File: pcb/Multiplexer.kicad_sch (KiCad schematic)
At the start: 1 part, among them U2 TMUX1308

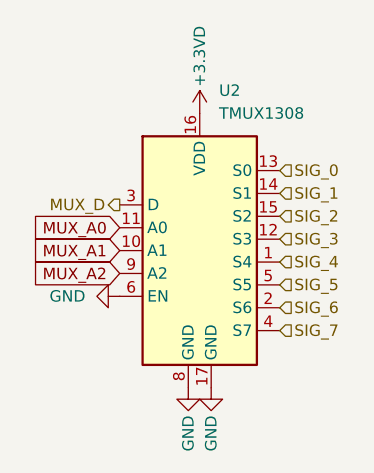
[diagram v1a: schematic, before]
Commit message: feat: assigned footprints for each symbol and switch
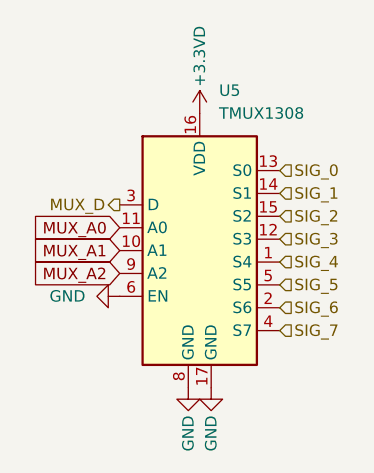
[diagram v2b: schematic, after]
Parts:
- renumbered U2 to U5
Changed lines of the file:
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@@
 		(on_board yes)
 		(dnp no)
-		(property "Reference" "#PWR05"
+		(property "Reference" "#PWR054"
 			(at 78.74 66.04 0)
 			(effects
@@
 			(project "prometheus-65"
 				(path "/7080535f-072d-4fc6-b033-a9cfe8594544/0adfa91a-0784-424f-9949-4c22152ab92f"
-					(reference "#PWR0513")
+					(reference "#PWR0448")
 					(unit 1)
 				)
 				(path "/7080535f-072d-4fc6-b033-a9cfe8594544/4aa91533-6d19-4b18-bd97-843bbf9a2ebd"
-					(reference "#PWR0517")
+					(reference "#PWR0452")
 					(unit 1)
 				)
 				(path "/7080535f-072d-4fc6-b033-a9cfe8594544/57499abe-bae0-4aba-b387-192b72537f00"
-					(reference "#PWR0285")
+					(reference "#PWR0252")
 					(unit 1)
 				)
 				(path "/7080535f-072d-4fc6-b033-a9cfe8594544/5fb3d5f1-a778-4ba7-9988-406cde0bb447"
-					(reference "#PWR0225")
+					(reference "#PWR0200")
 					(unit 1)
 				)
 				(path "/7080535f-072d-4fc6-b033-a9cfe8594544/8fd9d515-2105-4930-9563-b36413125d29"
-					(reference "#PWR0165")
+					(reference "#PWR0148")
 					(unit 1)
 				)
 				(path "/7080535f-072d-4fc6-b033-a9cfe8594544/a9c42e61-5ec1-4fa9-ae2f-cdc1de1fa9fe"
-					(reference "#PWR05")
+					(reference "#PWR054")
 					(unit 1)
 				)
 				(path "/7080535f-072d-4fc6-b033-a9cfe8594544/ea62a3f7-6568-4743-86d5-db015650f22d"
-					(reference "#PWR0521")
+					(reference "#PWR0456")
 					(unit 1)
 				)
 				(path "/7080535f-072d-4fc6-b033-a9cfe8594544/f2e1a5a1-adb9-4d0f-84af-2191946e6f18"
-					(reference "#PWR0525")
+					(reference "#PWR0460")
 					(unit 1)
 				)
@@
 		(dnp no)
 		(fields_autoplaced yes)
-		(property "Reference" "#PWR06"
+		(property "Reference" "#PWR055"
 			(at 63.5 82.55 0)
 			(effects
@@
 			(project "prometheus-65"
 				(path "/7080535f-072d-4fc6-b033-a9cfe8594544/0adfa91a-0784-424f-9949-4c22152ab92f"
-					(reference "#PWR0511")
+					(reference "#PWR0449")
 					(unit 1)
 				)
 				(path "/7080535f-072d-4fc6-b033-a9cfe8594544/4aa91533-6d19-4b18-bd97-843bbf9a2ebd"
-					(reference "#PWR0515")
+					(reference "#PWR0453")
 					(unit 1)
 				)
 				(path "/7080535f-072d-4fc6-b033-a9cfe8594544/57499abe-bae0-4aba-b387-192b72537f00"
-					(reference "#PWR0283")
+					(reference "#PWR0253")
 					(unit 1)
 				)
 				(path "/7080535f-072d-4fc6-b033-a9cfe8594544/5fb3d5f1-a778-4ba7-9988-406cde0bb447"
-					(reference "#PWR0223")
+					(reference "#PWR0201")
 					(unit 1)
 				)
 				(path "/7080535f-072d-4fc6-b033-a9cfe8594544/8fd9d515-2105-4930-9563-b36413125d29"
-					(reference "#PWR0163")
+					(reference "#PWR0149")
 					(unit 1)
 				)
 				(path "/7080535f-072d-4fc6-b033-a9cfe8594544/a9c42e61-5ec1-4fa9-ae2f-cdc1de1fa9fe"
-					(reference "#PWR06")
+					(reference "#PWR055")
 					(unit 1)
 				)
 				(path "/7080535f-072d-4fc6-b033-a9cfe8594544/ea62a3f7-6568-4743-86d5-db015650f22d"
-					(reference "#PWR0519")
+					(reference "#PWR0457")
 					(unit 1)
 				)
 				(path "/7080535f-072d-4fc6-b033-a9cfe8594544/f2e1a5a1-adb9-4d0f-84af-2191946e6f18"
-					(reference "#PWR0523")
+					(reference "#PWR0461")
 					(unit 1)
 				)
@@
 		(on_board yes)
 		(dnp no)
-		(property "Reference" "#PWR03"
+		(property "Reference" "#PWR056"
 			(at 77.47 99.06 0)
 			(effects
@@
 			(project "prometheus-65"
 				(path "/7080535f-072d-4fc6-b033-a9cfe8594544/0adfa91a-0784-424f-9949-4c22152ab92f"
-					(reference "#PWR0512")
+					(reference "#PWR0450")
 					(unit 1)
 				)
 				(path "/7080535f-072d-4fc6-b033-a9cfe8594544/4aa91533-6d19-4b18-bd97-843bbf9a2ebd"
-					(reference "#PWR0516")
+					(reference "#PWR0454")
 					(unit 1)
 				)
 				(path "/7080535f-072d-4fc6-b033-a9cfe8594544/57499abe-bae0-4aba-b387-192b72537f00"
-					(reference "#PWR0284")
+					(reference "#PWR0254")
 					(unit 1)
 				)
 				(path "/7080535f-072d-4fc6-b033-a9cfe8594544/5fb3d5f1-a778-4ba7-9988-406cde0bb447"
-					(reference "#PWR0224")
+					(reference "#PWR0202")
 					(unit 1)
 				)
 				(path "/7080535f-072d-4fc6-b033-a9cfe8594544/8fd9d515-2105-4930-9563-b36413125d29"
-					(reference "#PWR0164")
+					(reference "#PWR0150")
 					(unit 1)
 				)
 				(path "/7080535f-072d-4fc6-b033-a9cfe8594544/a9c42e61-5ec1-4fa9-ae2f-cdc1de1fa9fe"
-					(reference "#PWR03")
+					(reference "#PWR056")
 					(unit 1)
 				)
 				(path "/7080535f-072d-4fc6-b033-a9cfe8594544/ea62a3f7-6568-4743-86d5-db015650f22d"
-					(reference "#PWR0520")
+					(reference "#PWR0458")
 					(unit 1)
 				)
 				(path "/7080535f-072d-4fc6-b033-a9cfe8594544/f2e1a5a1-adb9-4d0f-84af-2191946e6f18"
-					(reference "#PWR0524")
+					(reference "#PWR0462")
 					(unit 1)
 				)
@@
 		(dnp no)
 		(fields_autoplaced yes)
-		(property "Reference" "U2"
+		(property "Reference" "U5"
 			(at 80.8833 59.69 0)
 			(effects
@@
 				)
 				(path "/7080535f-072d-4fc6-b033-a9cfe8594544/a9c42e61-5ec1-4fa9-ae2f-cdc1de1fa9fe"
-					(reference "U2")
+					(reference "U5")
 					(unit 1)
 				)
@@
 		(on_board yes)
 		(dnp no)
-		(property "Reference" "#PWR04"
+		(property "Reference" "#PWR057"
 			(at 80.01 99.06 0)
 			(effects
@@
 			(project "prometheus-65"
 				(path "/7080535f-072d-4fc6-b033-a9cfe8594544/0adfa91a-0784-424f-9949-4c22152ab92f"
-					(reference "#PWR0514")
+					(reference "#PWR0451")
 					(unit 1)
 				)
 				(path "/7080535f-072d-4fc6-b033-a9cfe8594544/4aa91533-6d19-4b18-bd97-843bbf9a2ebd"
-					(reference "#PWR0518")
+					(reference "#PWR0455")
 					(unit 1)
 				)
 				(path "/7080535f-072d-4fc6-b033-a9cfe8594544/57499abe-bae0-4aba-b387-192b72537f00"
-					(reference "#PWR0286")
+					(reference "#PWR0255")
 					(unit 1)
 				)
 				(path "/7080535f-072d-4fc6-b033-a9cfe8594544/5fb3d5f1-a778-4ba7-9988-406cde0bb447"
-					(reference "#PWR0226")
+					(reference "#PWR0203")
 					(unit 1)
 				)
 				(path "/7080535f-072d-4fc6-b033-a9cfe8594544/8fd9d515-2105-4930-9563-b36413125d29"
-					(reference "#PWR0166")
+					(reference "#PWR0151")
 					(unit 1)
 				)
 				(path "/7080535f-072d-4fc6-b033-a9cfe8594544/a9c42e61-5ec1-4fa9-ae2f-cdc1de1fa9fe"
-					(reference "#PWR04")
+					(reference "#PWR057")
 					(unit 1)
 				)
 				(path "/7080535f-072d-4fc6-b033-a9cfe8594544/ea62a3f7-6568-4743-86d5-db015650f22d"
-					(reference "#PWR0522")
+					(reference "#PWR0459")
 					(unit 1)
 				)
 				(path "/7080535f-072d-4fc6-b033-a9cfe8594544/f2e1a5a1-adb9-4d0f-84af-2191946e6f18"
-					(reference "#PWR0526")
-					(unit 1)
-				)
+					(reference "#PWR0463")
+					(unit 1)
+				)
